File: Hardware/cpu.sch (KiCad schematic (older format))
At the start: 20 parts, among them U13 STM32F411CEU6, Y2 Crystal_Small, Y3 Crystal_GND24

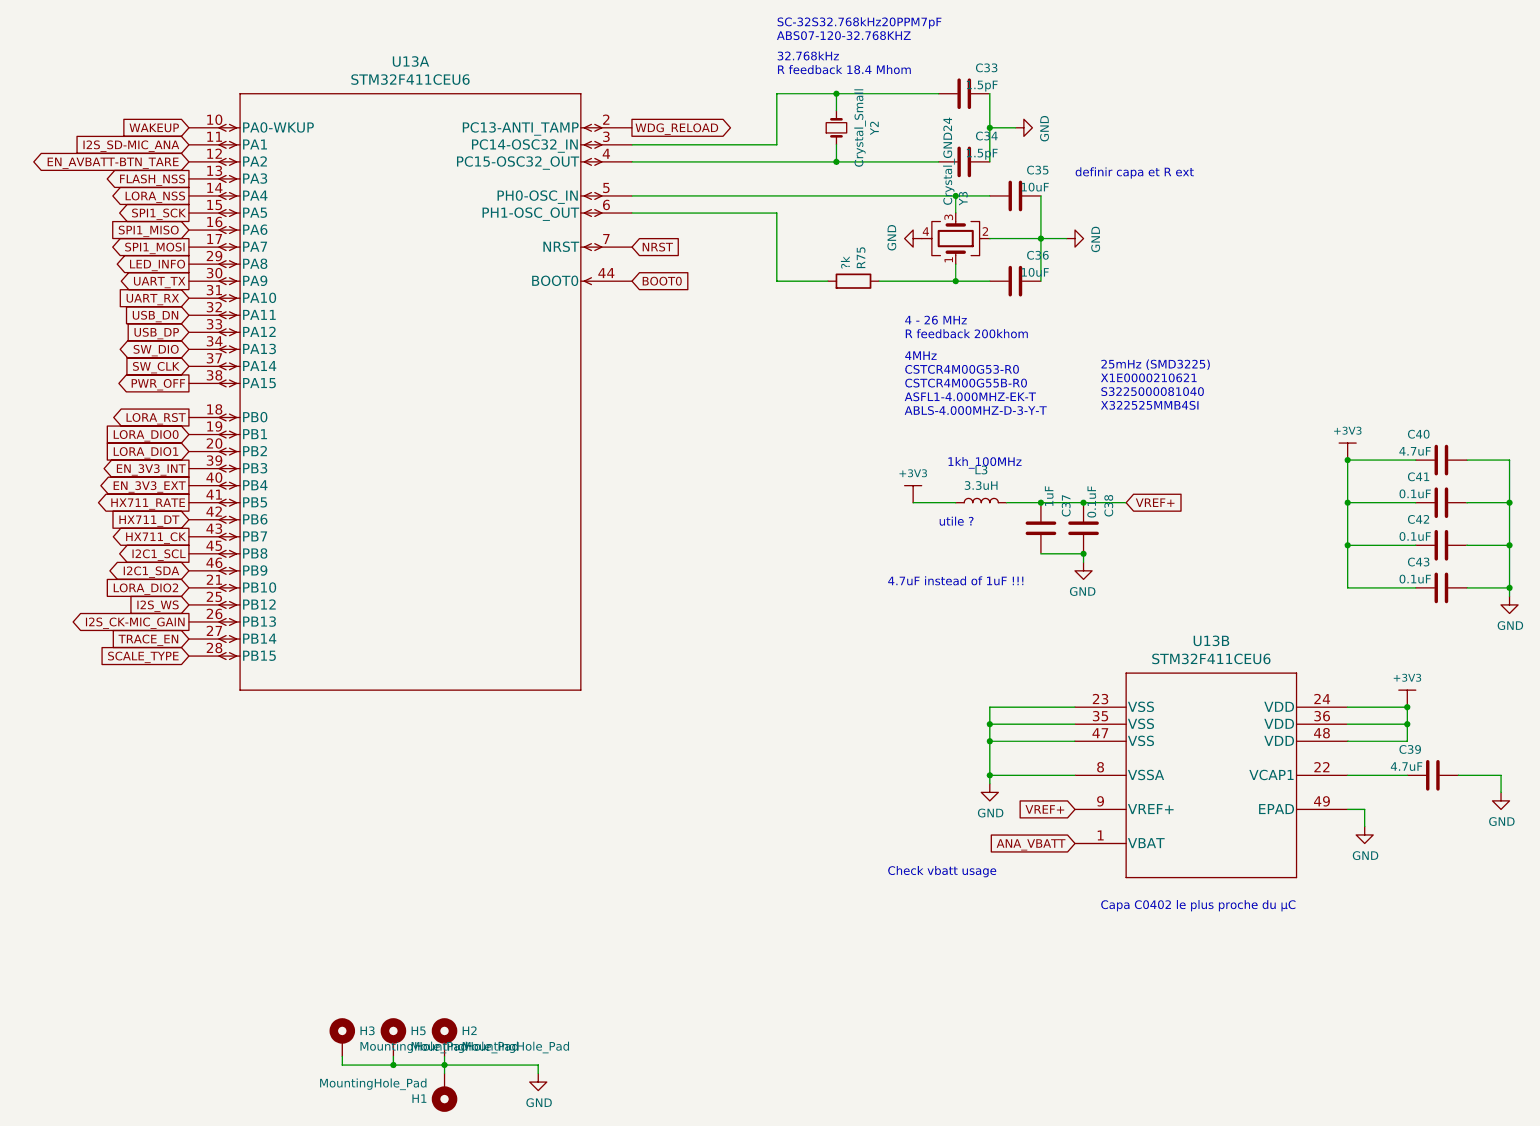
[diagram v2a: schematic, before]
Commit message: Add Gerber files, Bom, Jlcpcb LCSC parts ref, some optimizations
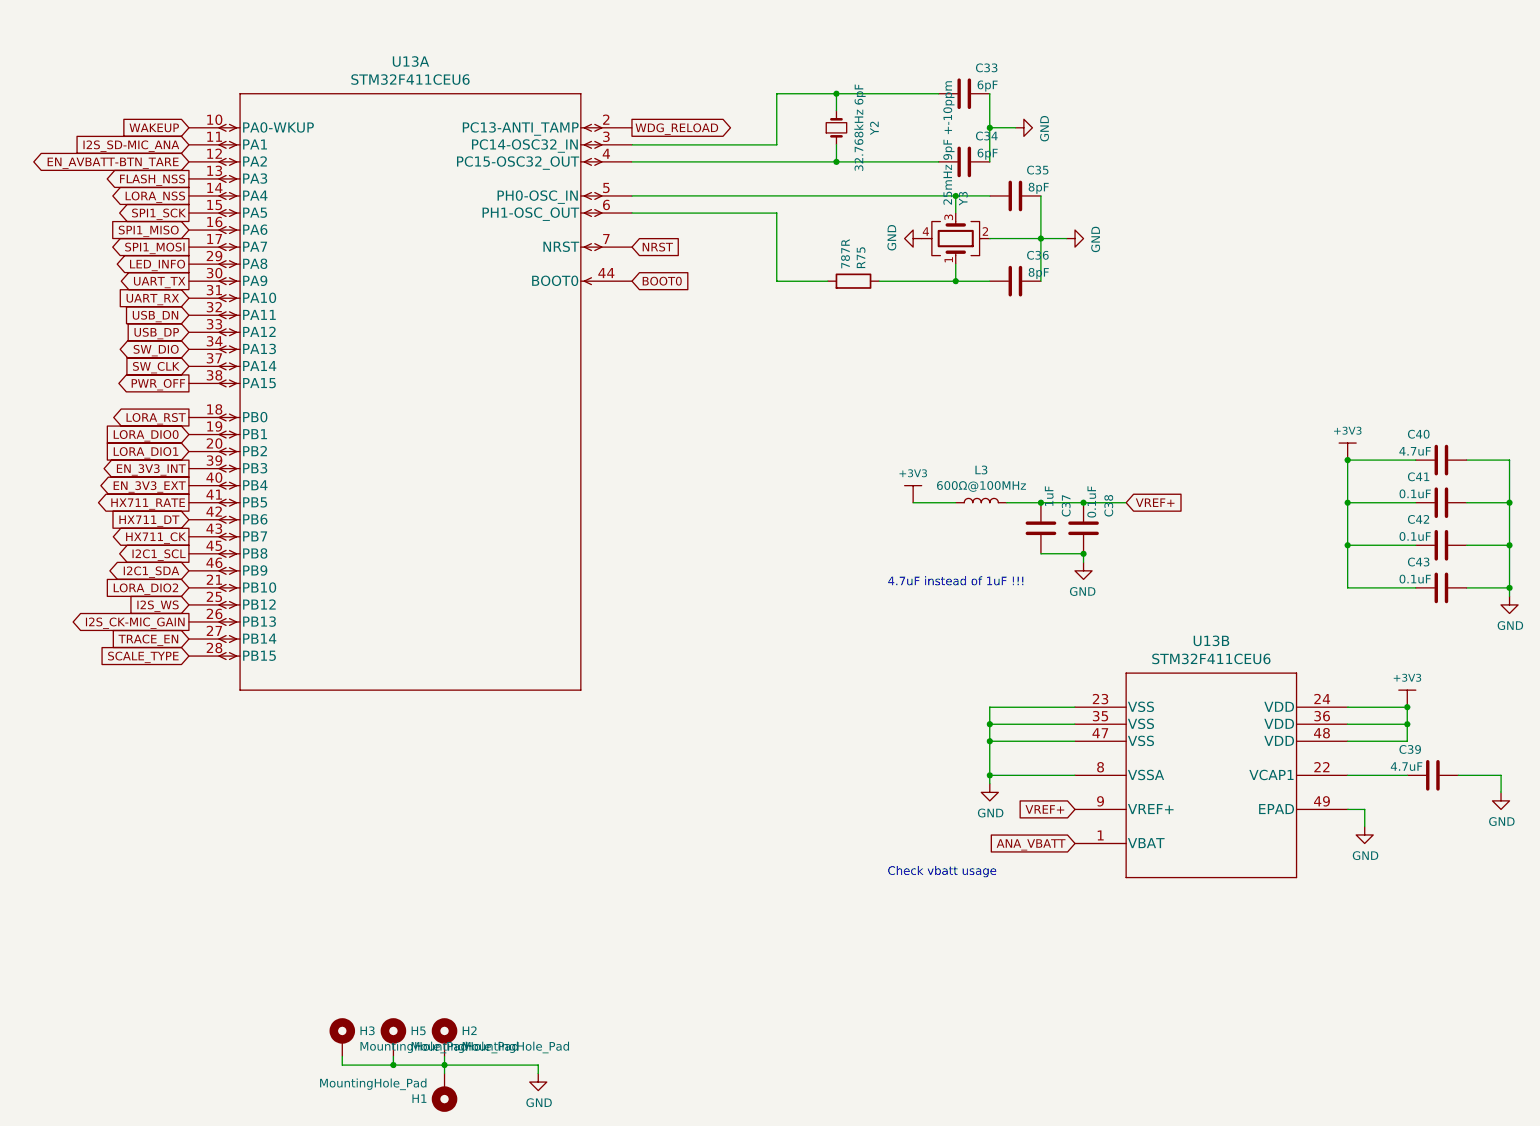
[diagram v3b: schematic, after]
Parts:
- C33, C34: value 1.5pF -> 6pF; Dielectric (none) -> C0G; JLC (none) -> 0201; LCSC (none) -> C161395; Manufacturer_Name (none) -> Murata Electronics; Manufacturer_Part_Number (none) -> GRM0335C1E6R0DA01D; Voltage (none) -> 25V
- C35, C36: value 10uF -> 8pF; Dielectric (none) -> C0G; JLC (none) -> 0201; LCSC (none) -> C161440; Manufacturer_Name (none) -> Murata Electronics; Manufacturer_Part_Number (none) -> GRM0335C1H8R0DA01D; Voltage (none) -> 50V
- C37: footprint Capacitor_SMD:C_0201_0603Metric -> Capacitor_SMD:C_0402_1005Metric; Dielectric (none) -> X7R; JLC (none) -> 0402; LCSC (none) -> C307427; Manufacturer_Name (none) -> Samsung Electro-Mechanics; Manufacturer_Part_Number (none) -> CL05B105KQ5NQNC; Size Inch 0201 -> 0402; Size Metric 0603 -> 1005; Tolerance (none) -> 10%; Voltage (none) -> 6.3V
- C38, C41, C42, C43: footprint Capacitor_SMD:C_0201_0603Metric -> Capacitor_SMD:C_0402_1005Metric; Dielectric (none) -> X7R; JLC (none) -> 0402; LCSC (none) -> C1525; Manufacturer_Name (none) -> Samsung Electro-Mechanics; Manufacturer_Part_Number (none) -> CL05B104KO5NNNC; Size Inch 0201 -> 0402; Size Metric 0603 -> 1005; Tolerance (none) -> 10%; Voltage (none) -> 16V
- C39, C40: footprint Capacitor_SMD:C_0201_0603Metric -> Capacitor_SMD:C_0402_1005Metric; Dielectric (none) -> X5R; JLC (none) -> 0402; LCSC (none) -> C77004; Manufacturer_Name (none) -> Murata Electronics; Manufacturer_Part_Number (none) -> GRM155R61A475KEAAD; Size Inch 0201 -> 0402; Size Metric 0603 -> 1005; Tolerance (none) -> 10%; Voltage (none) -> 10V
- L3: value 3.3uH -> 600Ω@100MHz; footprint Inductor_SMD:L_0402_1005Metric -> Inductor_SMD:L_0603_1608Metric; JLC (none) -> 0603; LCSC (none) -> C133937; Manufacturer_Name (none) -> TAI-TECH; Manufacturer_Part_Number (none) -> FCM1608KF-601T05; Size Inch (none) -> 0603; Size Metric (none) -> 1608; Tolerance (none) -> 25%
- R75: value ?k -> 787R; footprint Resistor_SMD:R_0201_0603Metric -> Resistor_SMD:R_0402_1005Metric; JLC (none) -> 0402; LCSC (none) -> C270582; Manufacturer_Name (none) -> UNI-ROYAL(Uniroyal Elec); Manufacturer_Part_Number (none) -> 0402WGF7870TCE; Power Rating (none) -> 1/16W; Size Inch 0201 -> 0402; Size Metric 0603 -> 1005; Voltage (none) -> 50V
- U13: JLC (none) -> UFQFPN-48; LCSC (none) -> C60420; Manufacturer_Name (none) -> STMicroelectronics; Manufacturer_Part_Number (none) -> STM32F411CEU6; package (none) -> UFQFPN-48
- Y2: value Crystal_Small -> 32.768kHz 6pF; JLC (none) -> 3215; LCSC (none) -> C2692145; Manufacturer_Name (none) -> Seiko; Manufacturer_Part_Number (none) -> SC-32S32.768kHz20PPM6pF; package (none) -> 3215_2P
- Y3: value Crystal_GND24 -> 25mHz 9pF +-10ppm; JLC (none) -> 3225; LCSC (none) -> C255920; Manufacturer_Name (none) -> Seiko Epson; Manufacturer_Part_Number (none) -> X1E0000210621
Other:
- note removed: "1kh_100MHz"
- note removed: "25mHz (SMD3225)\nX1E0000210621\nS3225000081040\nX322525MMB4SI\n\n"
- note removed: "32.768kHz\nR feedback 18.4 Mhom"
- note removed: "4 - 26 MHz\nR feedback 200khom"
- note removed: "4MHz\nCSTCR4M00G53-R0\nCSTCR4M00G55B-R0\nASFL1-4.000MHZ-EK-T\nABLS-4.000MHZ-D-3-Y-T"
- note removed: "Capa C0402 le plus proche du µC"
- note removed: "SC-32S32.768kHz20PPM7pF\nABS07-120-32.768KHZ"
- note removed: "definir capa et R ext"
- note removed: "utile ?"

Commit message: Fix JLCPCB assembly issues, Add reverse battery protection, Define Correct crystal capa, Add Layer number and fiducial, and some quicq fix
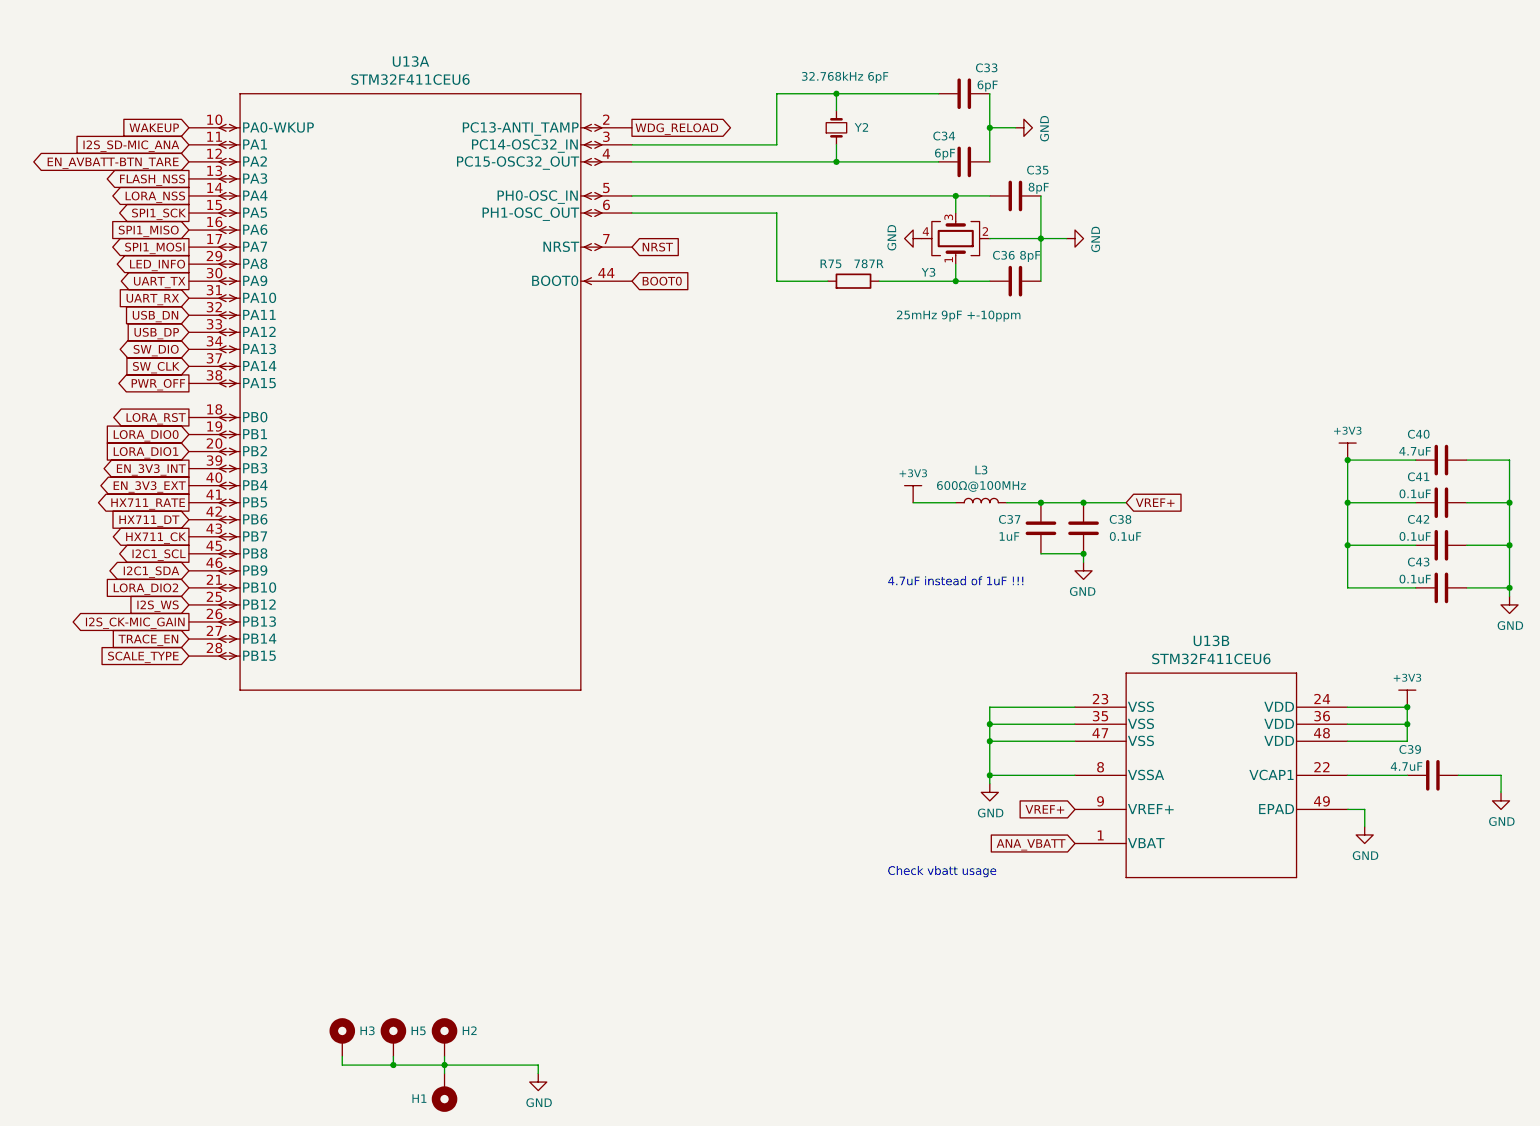
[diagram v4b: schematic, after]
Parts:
- C33, C34: footprint Capacitor_SMD:C_0201_0603Metric -> Capacitor_SMD:C_0402_1005Metric; JLC 0201 -> 0402; LCSC C161395 -> C437443; Manufacturer_Part_Number GRM0335C1E6R0DA01D -> GCM1555C1H6R0BA16D; Size Inch 0201 -> 0402; Size Metric 0603 -> 1005
- C35, C36: footprint Capacitor_SMD:C_0201_0603Metric -> Capacitor_SMD:C_0402_1005Metric; JLC 0201 -> 0402; LCSC C161440 -> C161335; Manufacturer_Part_Number GRM0335C1H8R0DA01D -> GJM1555C1H8R0BB01D; Size Inch 0201 -> 0402; Size Metric 0603 -> 1005
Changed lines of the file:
@@
 AR Path="/62B8145A/62BA86F0" Ref="H2"  Part="1"
 F 0 "H2" H 4150 6749 50  0000 L CNN
-F 1 "MountingHole_Pad" H 4150 6658 50  0000 L CNN
+F 1 "MountingHole_Pad" H 4050 6900 50  0001 L CNN
 F 2 "MountingHole:MountingHole_2.7mm_M2.5_Pad_Via" H 4050 6700 50  0001 C CNN
 F 3 "~" H 4050 6700 50  0001 C CNN
@@
 AR Path="/62B8145A/62BA86F6" Ref="H1"  Part="1"
 F 0 "H1" H 4150 7049 50  0000 L CNN
-F 1 "MountingHole_Pad" H 4150 6958 50  0000 L CNN
+F 1 "MountingHole_Pad" H 4150 6958 50  0001 L CNN
 F 2 "MountingHole:MountingHole_2.7mm_M2.5_Pad_Via" H 4050 7000 50  0001 C CNN
 F 3 "~" H 4050 7000 50  0001 C CNN
@@
 AR Path="/62EA3721/62BA87FA" Ref="C?"  Part="1"
 AR Path="/62B8145A/62BA87FA" Ref="C37"  Part="1"
-F 0 "C37" V 7700 3500 50  0000 L CNN
-F 1 "1uF" V 7600 3450 50  0000 L CNN
+F 0 "C37" H 7300 3650 50  0000 L CNN
+F 1 "1uF" H 7300 3750 50  0000 L CNN
 F 2 "Capacitor_SMD:C_0402_1005Metric" H 7588 3550 50  0001 C CNN
 F 3 "~" H 7550 3700 50  0001 C CNN
@@
 AR Path="/62EA3721/62BA87F4" Ref="C?"  Part="1"
 AR Path="/62B8145A/62BA87F4" Ref="C38"  Part="1"
-F 0 "C38" V 7950 3500 50  0000 L CNN
-F 1 "0.1uF" V 7850 3450 50  0000 L CNN
+F 0 "C38" H 7950 3650 50  0000 L CNN
+F 1 "0.1uF" H 7950 3750 50  0000 L CNN
 F 2 "Capacitor_SMD:C_0402_1005Metric" H 7838 3550 50  0001 C CNN
 F 3 "~" H 7800 3700 50  0001 C CNN
@@
 AR Path="/623CA958" Ref="Y?"  Part="1"
 AR Path="/62B8145A/623CA958" Ref="Y3"  Part="1"
-F 0 "Y3" H 7244 2046 50  0000 L CNN
-F 1 "25mHz 9pF +-10ppm" H 7244 1955 50  0000 L CNN
+F 0 "Y3" V 6850 1800 50  0000 L CNN
+F 1 "25mHz 9pF +-10ppm" V 6600 1650 50  0000 L CNN
 F 2 "EcoApi_pcb:X322525MMB4SI" H 7050 2000 50  0001 C CNN
 F 3 "~" H 7050 2000 50  0001 C CNN
@@
 F 0 "C35" V 7550 1550 50  0000 L CNN
 F 1 "8pF" V 7450 1550 50  0000 L CNN
-F 2 "Capacitor_SMD:C_0201_0603Metric" H 7438 1600 50  0001 C CNN
+F 2 "Capacitor_SMD:C_0402_1005Metric" H 7438 1600 50  0001 C CNN
 F 3 "~" H 7400 1750 50  0001 C CNN
 F 4 "yes" H 7400 1750 50  0001 C CNN "Populate"
-F 5 "0201" H 7400 1750 50  0001 C CNN "Size Inch"
-F 6 "0603" H 7400 1750 50  0001 C CNN "Size Metric"
+F 5 "0402" H 7400 1750 50  0001 C CNN "Size Inch"
+F 6 "1005" H 7400 1750 50  0001 C CNN "Size Metric"
 F 7 "C0G" H 7400 1750 50  0001 C CNN "Dielectric"
-F 8 "0201" H 7400 1750 50  0001 C CNN "JLC"
-F 9 "C161440" H 7400 1750 50  0001 C CNN "LCSC"
+F 8 "0402" H 7400 1750 50  0001 C CNN "JLC"
+F 9 "C161335" H 7400 1750 50  0001 C CNN "LCSC"
 F 10 "Murata Electronics" H 7400 1750 50  0001 C CNN "Manufacturer_Name"
-F 11 "GRM0335C1H8R0DA01D" H 7400 1750 50  0001 C CNN "Manufacturer_Part_Number"
+F 11 "GJM1555C1H8R0BB01D" H 7400 1750 50  0001 C CNN "Manufacturer_Part_Number"
 F 12 "50V" H 7400 1750 50  0001 C CNN "Voltage"
 	1    7400 1750
@@
 AR Path="/623CA944" Ref="C?"  Part="1"
 AR Path="/62B8145A/623CA944" Ref="C36"  Part="1"
-F 0 "C36" V 7550 2050 50  0000 L CNN
-F 1 "8pF" V 7450 2050 50  0000 L CNN
-F 2 "Capacitor_SMD:C_0201_0603Metric" H 7438 2100 50  0001 C CNN
+F 0 "C36" V 7550 2250 50  0000 L CNN
+F 1 "8pF" V 7550 2100 50  0000 L CNN
+F 2 "Capacitor_SMD:C_0402_1005Metric" H 7438 2100 50  0001 C CNN
 F 3 "~" H 7400 2250 50  0001 C CNN
 F 4 "yes" H 7400 2250 50  0001 C CNN "Populate"
-F 5 "0201" H 7400 2250 50  0001 C CNN "Size Inch"
-F 6 "0603" H 7400 2250 50  0001 C CNN "Size Metric"
+F 5 "0402" H 7400 2250 50  0001 C CNN "Size Inch"
+F 6 "1005" H 7400 2250 50  0001 C CNN "Size Metric"
 F 7 "C0G" H 7400 2250 50  0001 C CNN "Dielectric"
-F 8 "0201" H 7400 2250 50  0001 C CNN "JLC"
-F 9 "C161440" H 7400 2250 50  0001 C CNN "LCSC"
+F 8 "0402" H 7400 2250 50  0001 C CNN "JLC"
+F 9 "C161335" H 7400 2250 50  0001 C CNN "LCSC"
 F 10 "Murata Electronics" H 7400 2250 50  0001 C CNN "Manufacturer_Name"
-F 11 "GRM0335C1H8R0DA01D" H 7400 2250 50  0001 C CNN "Manufacturer_Part_Number"
+F 11 "GJM1555C1H8R0BB01D" H 7400 2250 50  0001 C CNN "Manufacturer_Part_Number"
 F 12 "50V" H 7400 2250 50  0001 C CNN "Voltage"
 	1    7400 2250
@@
 AR Path="/623CA93C" Ref="R?"  Part="1"
 AR Path="/62B8145A/623CA93C" Ref="R75"  Part="1"
-F 0 "R75" H 6520 2296 50  0000 L CNN
-F 1 "787R" H 6520 2205 50  0000 L CNN
+F 0 "R75" V 6550 2050 50  0000 L CNN
+F 1 "787R" V 6550 2250 50  0000 L CNN
 F 2 "Resistor_SMD:R_0402_1005Metric" V 6380 2250 50  0001 C CNN
 F 3 "~" H 6450 2250 50  0001 C CNN
@@
 AR Path="/62365F90" Ref="Y?"  Part="1"
 AR Path="/62B8145A/62365F90" Ref="Y2"  Part="1"
-F 0 "Y2" H 6350 1575 50  0000 C CNN
-F 1 "32.768kHz 6pF" H 6350 1484 50  0000 C CNN
+F 0 "Y2" V 6350 1500 50  0000 C CNN
+F 1 "32.768kHz 6pF" V 6650 1400 50  0000 C CNN
 F 2 "EcoApi_pcb:XTAL_ABS07-120-32.768KHZ-T" H 6350 1350 50  0001 C CNN
 F 3 "~" H 6350 1350 50  0001 C CNN
@@
 AR Path="/62365FCD" Ref="C?"  Part="1"
 AR Path="/62B8145A/62365FCD" Ref="C34"  Part="1"
-F 0 "C34" V 7250 1350 50  0000 L CNN
-F 1 "6pF" V 7150 1350 50  0000 L CNN
-F 2 "Capacitor_SMD:C_0201_0603Metric" H 7138 1400 50  0001 C CNN
+F 0 "C34" V 7250 1600 50  0000 L CNN
+F 1 "6pF" V 7150 1600 50  0000 L CNN
+F 2 "Capacitor_SMD:C_0402_1005Metric" H 7138 1400 50  0001 C CNN
 F 3 "~" H 7100 1550 50  0001 C CNN
 F 4 "yes" H 7100 1550 50  0001 C CNN "Populate"
-F 5 "0201" H 7100 1550 50  0001 C CNN "Size Inch"
-F 6 "0603" H 7100 1550 50  0001 C CNN "Size Metric"
+F 5 "0402" H 7100 1550 50  0001 C CNN "Size Inch"
+F 6 "1005" H 7100 1550 50  0001 C CNN "Size Metric"
 F 7 "C0G" H 7100 1550 50  0001 C CNN "Dielectric"
-F 8 "0201" H 7100 1550 50  0001 C CNN "JLC"
-F 9 "C161395" H 7100 1550 50  0001 C CNN "LCSC"
+F 8 "0402" H 7100 1550 50  0001 C CNN "JLC"
+F 9 "C437443" H 7100 1550 50  0001 C CNN "LCSC"
 F 10 "Murata Electronics" H 7100 1550 50  0001 C CNN "Manufacturer_Name"
-F 11 "GRM0335C1E6R0DA01D" H 7100 1550 50  0001 C CNN "Manufacturer_Part_Number"
+F 11 "GCM1555C1H6R0BA16D" H 7100 1550 50  0001 C CNN "Manufacturer_Part_Number"
 F 12 "25V" H 7100 1550 50  0001 C CNN "Voltage"
 	1    7100 1550
@@
 F 0 "C33" V 7250 950 50  0000 L CNN
 F 1 "6pF" V 7150 950 50  0000 L CNN
-F 2 "Capacitor_SMD:C_0201_0603Metric" H 7138 1000 50  0001 C CNN
+F 2 "Capacitor_SMD:C_0402_1005Metric" H 7138 1000 50  0001 C CNN
 F 3 "~" H 7100 1150 50  0001 C CNN
 F 4 "yes" H 7100 1150 50  0001 C CNN "Populate"
-F 5 "0201" H 7100 1150 50  0001 C CNN "Size Inch"
-F 6 "0603" H 7100 1150 50  0001 C CNN "Size Metric"
+F 5 "0402" H 7100 1150 50  0001 C CNN "Size Inch"
+F 6 "1005" H 7100 1150 50  0001 C CNN "Size Metric"
 F 7 "C0G" H 7100 1150 50  0001 C CNN "Dielectric"
-F 8 "0201" H 7100 1150 50  0001 C CNN "JLC"
-F 9 "C161395" H 7100 1150 50  0001 C CNN "LCSC"
+F 8 "0402" H 7100 1150 50  0001 C CNN "JLC"
+F 9 "C437443" H 7100 1150 50  0001 C CNN "LCSC"
 F 10 "Murata Electronics" H 7100 1150 50  0001 C CNN "Manufacturer_Name"
-F 11 "GRM0335C1E6R0DA01D" H 7100 1150 50  0001 C CNN "Manufacturer_Part_Number"
+F 11 "GCM1555C1H6R0BA16D" H 7100 1150 50  0001 C CNN "Manufacturer_Part_Number"
 F 12 "25V" H 7100 1150 50  0001 C CNN "Voltage"
 	1    7100 1150
@@
 AR Path="/62B8145A/63B128D4" Ref="H3"  Part="1"
 F 0 "H3" H 3550 6749 50  0000 L CNN
-F 1 "MountingHole_Pad" H 3550 6658 50  0000 L CNN
+F 1 "MountingHole_Pad" H 3550 6658 50  0001 L CNN
 F 2 "MountingHole:MountingHole_2.7mm_M2.5_Pad_Via" H 3450 6700 50  0001 C CNN
 F 3 "~" H 3450 6700 50  0001 C CNN
@@
 AR Path="/62B8145A/63B14935" Ref="H5"  Part="1"
 F 0 "H5" H 3850 6749 50  0000 L CNN
-F 1 "MountingHole_Pad" H 3850 6658 50  0000 L CNN
+F 1 "MountingHole_Pad" H 3300 6950 50  0001 L CNN
 F 2 "MountingHole:MountingHole_2.7mm_M2.5_Pad_Via" H 3750 6700 50  0001 C CNN
 F 3 "~" H 3750 6700 50  0001 C CNN

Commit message: Debug some features on hardware
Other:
- note added: "enlever wakeup"
- note added: "enlever wdg reload"
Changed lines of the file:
@@
 Wire Wire Line
 	6000 2250 6300 2250
+Text Notes 2100 1200 0    50   ~ 0
+enlever wakeup
+Text Notes 5050 1200 0    50   ~ 0
+enlever wdg reload
 $EndSCHEMATC
